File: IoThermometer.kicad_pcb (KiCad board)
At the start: 2 copper layers, 82.6 x 33 mm, 11 parts, among them U1 NodeMCU_Amica_R2, U2 DS18B20

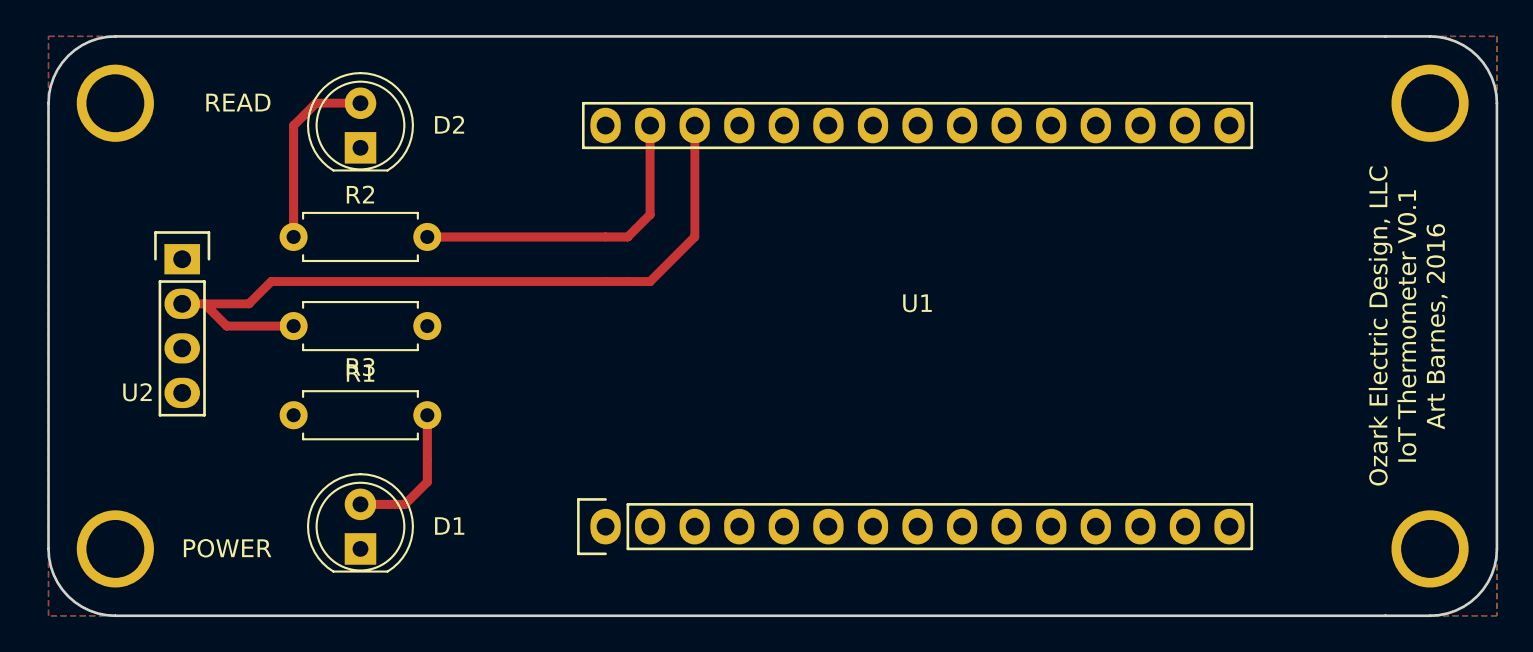
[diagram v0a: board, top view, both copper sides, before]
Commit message: edited silkscreen
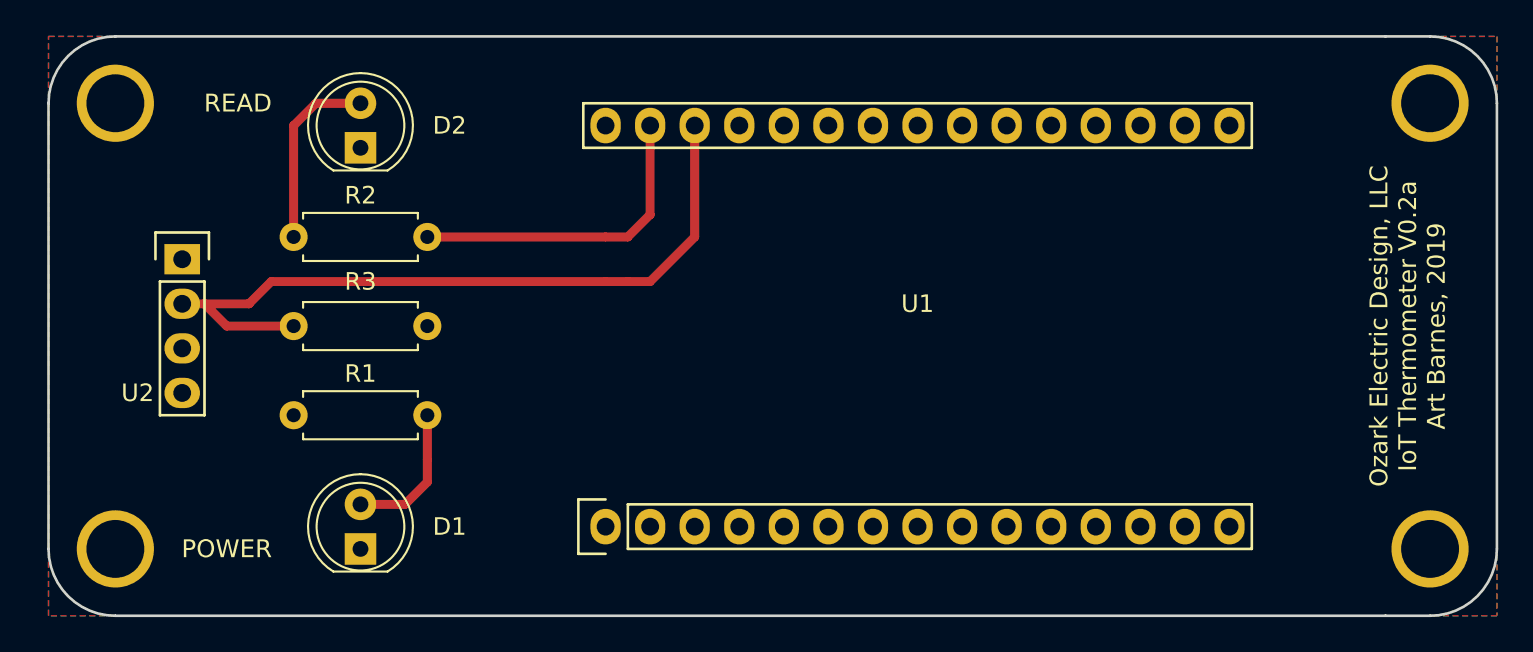
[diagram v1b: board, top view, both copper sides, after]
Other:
- board text added: "Ozark Electric Design, LLC IoT Thermometer V0.2a Art Barnes, 2019"
- board text removed: "Ozark Electric Design, LLC IoT Thermometer V0.1 Art Barnes, 2016"
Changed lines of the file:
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@@
   )
   (layers
-    (0 F.Cu signal)
+    (0 F.Cu signal hide)
     (31 B.Cu signal hide)
     (32 B.Adhes user)
@@
   )
   (setup
-    (last_trace_width 0.508)
+    (last_trace_width 0.254)
     (user_trace_width 0.254)
     (user_trace_width 0.508)
@@
     (descr "Resistor, Axial_DIN0207 series, Axial, Horizontal, pin pitch=7.62mm, 0.25W = 1/4W, length*diameter=6.3*2.5mm^2, http://cdn-reichelt.de/documents/datenblatt/B400/1_4W%23YAG.pdf")
     (tags "Resistor Axial_DIN0207 series Axial Horizontal pin pitch 7.62mm 0.25W = 1/4W length 6.3mm diameter 2.5mm")
-    (fp_text reference R3 (at 3.81 -2.37 180) (layer F.SilkS)
+    (fp_text reference R3 (at 3.81 2.54 180) (layer F.SilkS)
       (effects (font (size 1 1) (thickness 0.15)))
     )
@@
     (effects (font (size 1.016 1.016) (thickness 0.1905)))
   )
-  (gr_text "Ozark Electric Design, LLC\nIoT Thermometer V0.1\nArt Barnes, 2016\n" (at 182.69 107.57 90) (layer F.SilkS)
+  (gr_text "Ozark Electric Design, LLC\nIoT Thermometer V0.2a\nArt Barnes, 2019\n" (at 182.69 107.57 90) (layer F.SilkS)
     (effects (font (size 1.016 1.016) (thickness 0.1905)))
   )

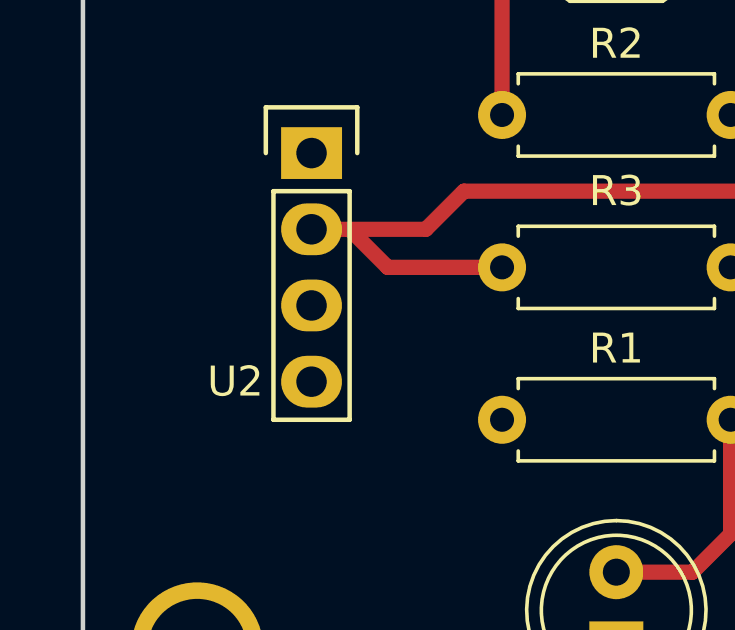
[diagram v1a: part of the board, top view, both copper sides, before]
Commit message: change dht22 symbol, fix pinout in footprint
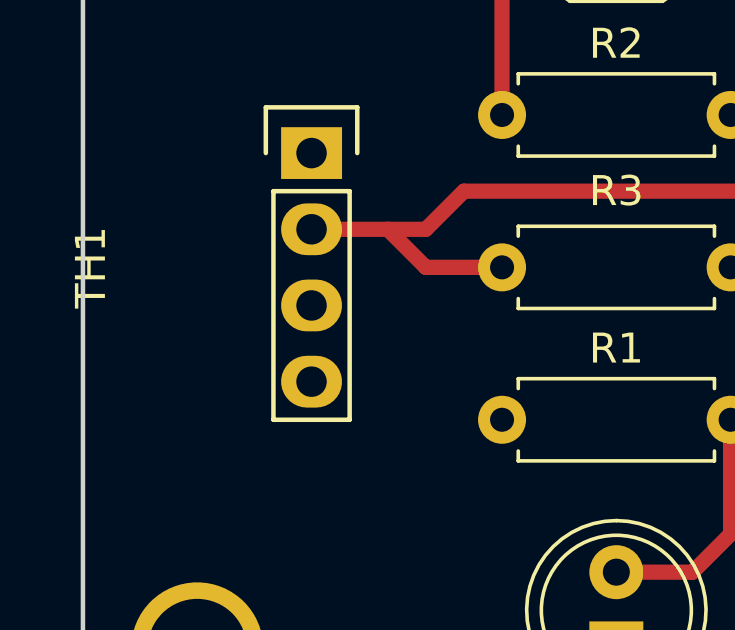
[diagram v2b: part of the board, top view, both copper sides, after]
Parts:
- removed U2: DS18B20, Sensors:DHT22_Temperature_Humidity
- added TH1: DHT22_Temperature_Humidity, Sensors:DHT22_Temperature_Humidity, F.Cu at (112.8, 107.6)
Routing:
- net Net-(R3-Pad2): track 42.7 -> 41.5 mm
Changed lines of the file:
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@@
     (zones 0)
     (modules 11)
-    (nets 28)
+    (nets 29)
   )
   (page A4)
@@
   )
   (layers
-    (0 F.Cu signal hide)
-    (31 B.Cu signal hide)
+    (0 F.Cu signal)
+    (31 B.Cu signal)
     (32 B.Adhes user)
     (33 F.Adhes user)
@@
     (35 F.Paste user)
     (36 B.SilkS user)
-    (37 F.SilkS user)
+    (37 F.SilkS user hide)
     (38 B.Mask user)
     (39 F.Mask user)
@@
   (net 26 "Net-(U1-Pad26)")
   (net 27 "Net-(U1-Pad21)")
+  (net 28 "Net-(TH1-Pad3)")
   (net_class Default "This is the default net class."
     (clearance 0.254)
@@
     (add_net "Net-(R2-Pad2)")
     (add_net "Net-(R3-Pad2)")
+    (add_net "Net-(TH1-Pad3)")
     (add_net "Net-(U1-Pad1)")
     (add_net "Net-(U1-Pad12)")
@@
     )
   )
-  (module Sensors:DHT22_Temperature_Humidity placed (layer F.Cu)
-    (at 112.84 107.57 270)
-    (fp_text reference U2 (at 3.81 2.54 180) (layer F.SilkS)
-      (effects (font (size 1 1) (thickness 0.15)))
-    )
-    (fp_text value DS18B20 (at -2.54 2.54 90) (layer F.Fab)
-      (effects (font (size 1 1) (thickness 0.15)))
-    )
-    (fp_line (start -2.54 1.27) (end -2.54 -1.27) (layer F.SilkS) (width 0.15))
-    (fp_line (start 5.08 1.27) (end -2.54 1.27) (layer F.SilkS) (width 0.15))
-    (fp_line (start 5.08 -1.27) (end 5.08 1.27) (layer F.SilkS) (width 0.15))
-    (fp_line (start -2.54 -1.27) (end 5.08 -1.27) (layer F.SilkS) (width 0.15))
-    (fp_line (start -5.334 1.524) (end -3.81 1.524) (layer F.SilkS) (width 0.15))
-    (fp_line (start -5.334 -1.524) (end -5.334 1.524) (layer F.SilkS) (width 0.15))
-    (fp_line (start -3.81 -1.524) (end -5.334 -1.524) (layer F.SilkS) (width 0.15))
-    (fp_line (start -7.62 4.3) (end 7.62 4.3) (layer B.CrtYd) (width 0.15))
-    (fp_line (start -7.62 -3.3) (end -7.62 4.3) (layer B.CrtYd) (width 0.15))
-    (fp_line (start 7.62 -3.3) (end 7.62 4.3) (layer B.CrtYd) (width 0.15))
-    (fp_line (start -7.62 -3.3) (end 7.62 -3.3) (layer B.CrtYd) (width 0.15))
-    (fp_line (start -7.62 -2) (end 7.62 -2) (layer B.CrtYd) (width 0.15))
-    (pad 1 thru_hole rect (at -3.81 0) (size 2.032 1.7272) (drill 1.016) (layers *.Cu *.Mask F.SilkS)
-      (net 2 GND))
-    (pad 2 thru_hole oval (at -1.27 0) (size 2.032 1.7272) (drill 1.016) (layers *.Cu *.Mask F.SilkS)
-      (net 25 "Net-(R3-Pad2)"))
-    (pad 3 thru_hole oval (at 1.27 0) (size 2.032 1.7272) (drill 1.016) (layers *.Cu *.Mask F.SilkS)
-      (net 4 +3V3))
-    (pad 4 thru_hole oval (at 3.81 0) (size 2.032 1.7272) (drill 1.016) (layers *.Cu *.Mask F.SilkS))
-  )
   (module LED_THT:LED_D5.0mm (layer F.Cu)
     (at 123 120.27 90)
@@
     )
   )
+  (module Sensors:DHT22_Temperature_Humidity (layer F.Cu)
+    (at 112.84 107.57 270)
+    (fp_text reference TH1 (at 0 7.35 90) (layer F.SilkS)
+      (effects (font (size 1 1) (thickness 0.15)))
+    )
+    (fp_text value DHT22_Temperature_Humidity (at 0 5.445 90) (layer F.Fab) hide
+      (effects (font (size 1 1) (thickness 0.15)))
+    )
+    (fp_line (start -2.54 1.27) (end -2.54 -1.27) (layer F.SilkS) (width 0.15))
+    (fp_line (start 5.08 1.27) (end -2.54 1.27) (layer F.SilkS) (width 0.15))
+    (fp_line (start 5.08 -1.27) (end 5.08 1.27) (layer F.SilkS) (width 0.15))
+    (fp_line (start -2.54 -1.27) (end 5.08 -1.27) (layer F.SilkS) (width 0.15))
+    (fp_line (start -5.334 1.524) (end -3.81 1.524) (layer F.SilkS) (width 0.15))
+    (fp_line (start -5.334 -1.524) (end -5.334 1.524) (layer F.SilkS) (width 0.15))
+    (fp_line (start -3.81 -1.524) (end -5.334 -1.524) (layer F.SilkS) (width 0.15))
+    (fp_line (start -7.62 4.3) (end 7.62 4.3) (layer B.CrtYd) (width 0.15))
+    (fp_line (start -7.62 -3.3) (end -7.62 4.3) (layer B.CrtYd) (width 0.15))
+    (fp_line (start 7.62 -3.3) (end 7.62 4.3) (layer B.CrtYd) (width 0.15))
+    (fp_line (start -7.62 -3.3) (end 7.62 -3.3) (layer B.CrtYd) (width 0.15))
+    (fp_line (start -7.62 -2) (end 7.62 -2) (layer B.CrtYd) (width 0.15))
+    (pad 1 thru_hole rect (at -3.81 0) (size 2.032 1.7272) (drill 1.016) (layers *.Cu *.Mask F.SilkS)
+      (net 4 +3V3))
+    (pad 2 thru_hole oval (at -1.27 0) (size 2.032 1.7272) (drill 1.016) (layers *.Cu *.Mask F.SilkS)
+      (net 25 "Net-(R3-Pad2)"))
+    (pad 3 thru_hole oval (at 1.27 0) (size 2.032 1.7272) (drill 1.016) (layers *.Cu *.Mask F.SilkS)
+      (net 28 "Net-(TH1-Pad3)"))
+    (pad 4 thru_hole oval (at 3.81 0) (size 2.032 1.7272) (drill 1.016) (layers *.Cu *.Mask F.SilkS)
+      (net 2 GND))
+  )
   (gr_line (start 181.42 124.08) (end 183.96 124.08) (angle 90) (layer Edge.Cuts) (width 0.15))
   (gr_line (start 181.42 91.06) (end 183.96 91.06) (angle 90) (layer Edge.Cuts) (width 0.15))
@@
   (segment (start 136.97 102.49) (end 138.24 102.49) (width 0.508) (layer F.Cu) (net 5))
   (segment (start 112.84 106.3) (end 114.11 106.3) (width 0.508) (layer F.Cu) (net 25) (status 400000))
-  (segment (start 119.19 107.57) (end 115.38 107.57) (width 0.508) (layer F.Cu) (net 25) (status 400000))
-  (segment (start 115.38 107.57) (end 114.11 106.3) (width 0.508) (layer F.Cu) (net 25))
   (segment (start 114.11 106.3) (end 116.65 106.3) (width 0.508) (layer F.Cu) (net 25))
   (segment (start 142.05 102.49) (end 142.05 96.14) (width 0.508) (layer F.Cu) (net 25) (status 800000))
@@
   (segment (start 138.24 105.03) (end 139.51 105.03) (width 0.508) (layer F.Cu) (net 25))
   (segment (start 139.51 105.03) (end 142.05 102.49) (width 0.508) (layer F.Cu) (net 25))
+  (segment (start 116.65 107.57) (end 115.38 106.3) (width 0.508) (layer F.Cu) (net 25))
+  (segment (start 119.19 107.57) (end 116.65 107.57) (width 0.508) (layer F.Cu) (net 25))
   (zone (net 2) (net_name GND) (layer B.Cu) (hatch edge 0.508)
     (connect_pads (clearance 0.508))

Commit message: adjust layer visibility
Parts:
- renumbered TH1 to DHT22
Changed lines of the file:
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@@
   )
   (layers
-    (0 F.Cu signal)
-    (31 B.Cu signal)
-    (32 B.Adhes user)
-    (33 F.Adhes user)
-    (34 B.Paste user)
-    (35 F.Paste user)
+    (0 F.Cu signal hide)
+    (31 B.Cu signal hide)
+    (32 B.Adhes user hide)
+    (33 F.Adhes user hide)
+    (34 B.Paste user hide)
+    (35 F.Paste user hide)
     (36 B.SilkS user)
-    (37 F.SilkS user hide)
+    (37 F.SilkS user)
     (38 B.Mask user)
     (39 F.Mask user)
@@
       (effects (font (size 1 1) (thickness 0.15)))
     )
-    (fp_text value LED (at 1.27 3.96 90) (layer F.Fab)
+    (fp_text value LED (at 2.54 -5.08 90) (layer F.Fab)
       (effects (font (size 1 1) (thickness 0.15)))
     )
@@
       (effects (font (size 1 1) (thickness 0.15)))
     )
-    (fp_text value LED (at 1.27 3.96 90) (layer F.Fab)
+    (fp_text value LED (at -1.27 -5.08 90) (layer F.Fab)
       (effects (font (size 1 1) (thickness 0.15)))
     )
@@
   (module Sensors:DHT22_Temperature_Humidity (layer F.Cu)
     (at 112.84 107.57 270)
-    (fp_text reference TH1 (at 0 7.35 90) (layer F.SilkS)
+    (fp_text reference DHT22 (at 0 5.08 90) (layer F.SilkS)
       (effects (font (size 1 1) (thickness 0.15)))
     )
@@
   (segment (start 116.65 107.57) (end 115.38 106.3) (width 0.508) (layer F.Cu) (net 25))
   (segment (start 119.19 107.57) (end 116.65 107.57) (width 0.508) (layer F.Cu) (net 25))
-  (zone (net 2) (net_name GND) (layer B.Cu) (hatch edge 0.508)
+  (zone (net 4) (net_name +3V3) (layer F.Cu) (hatch edge 0.508)
     (connect_pads (clearance 0.508))
     (min_thickness 0.254)
@@
     )
   )
-  (zone (net 4) (net_name +3V3) (layer F.Cu) (hatch edge 0.508)
+  (zone (net 2) (net_name GND) (layer B.Cu) (hatch edge 0.508)
     (connect_pads (clearance 0.508))
     (min_thickness 0.254)

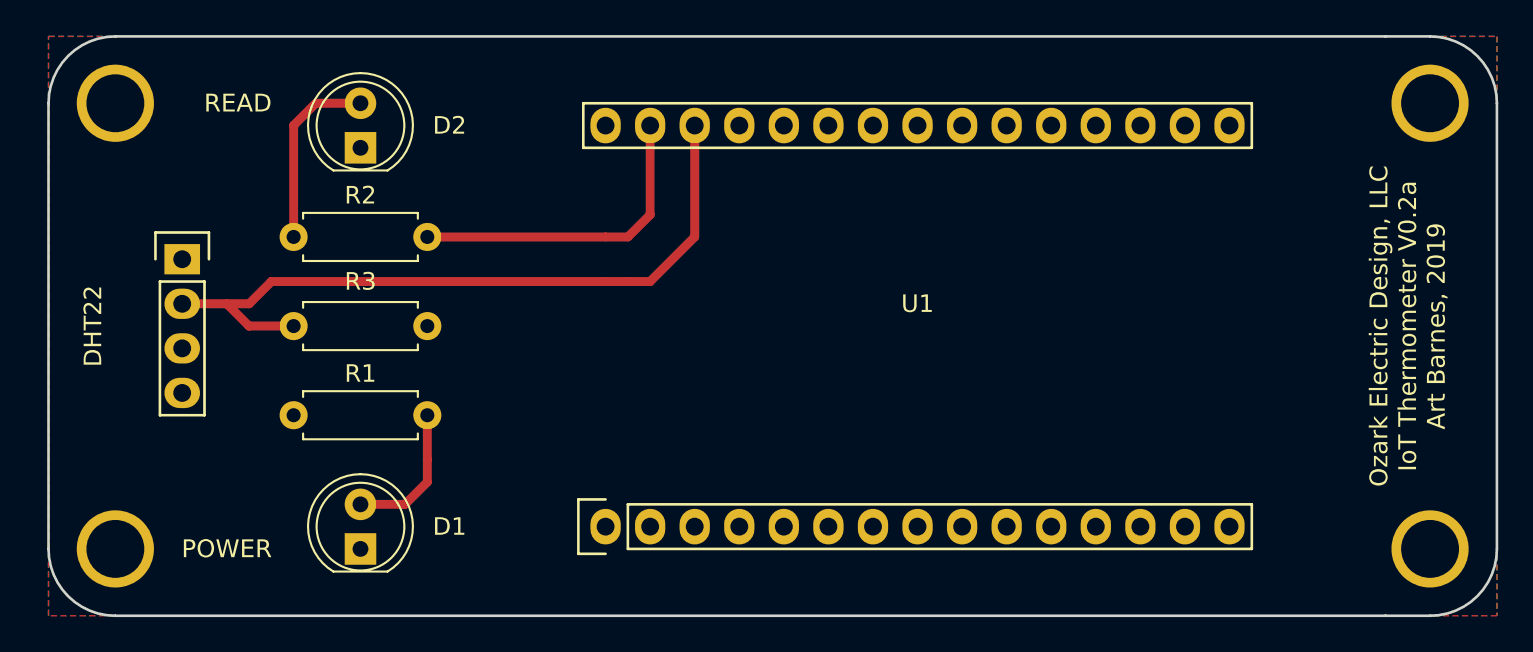
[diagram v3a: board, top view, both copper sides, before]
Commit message: resize resistors & change about text
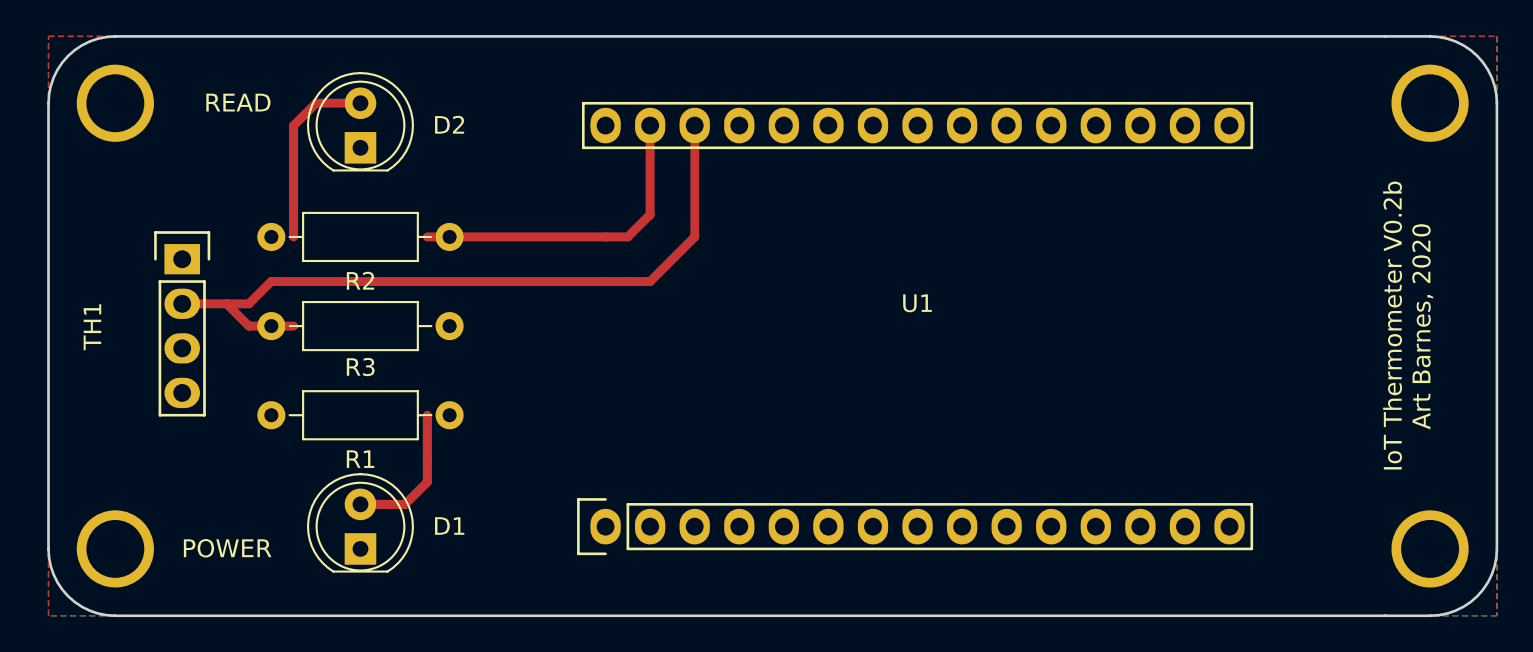
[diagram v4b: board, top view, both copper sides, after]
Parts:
- R1, R2, R3: footprint Resistor_THT:R_Axial_DIN0207_L6.3mm_D2.5mm_P7.62mm_Horizontal -> Resistor_THT:R_Axial_DIN0207_L6.3mm_D2.5mm_P10.16mm_Horizontal
- moved R3 1.27 mm to (128.1, 107.6)
- moved R1 1.27 mm to (117.9, 112.7)
- moved R2 1.27 mm to (117.9, 102.5)
- renumbered DHT22 to TH1
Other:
- board text added: "IoT Thermometer V0.2b Art Barnes, 2020"
- board text removed: "Ozark Electric Design, LLC IoT Thermometer V0.2a Art Barnes, 2019"
